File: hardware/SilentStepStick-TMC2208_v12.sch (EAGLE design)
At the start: 26 parts, among them IC1 TMC2208, J1 JUMPER2-0402, J2 JUMPER3-0402-NC, X1 PASSER-04, X2 PASSER-04

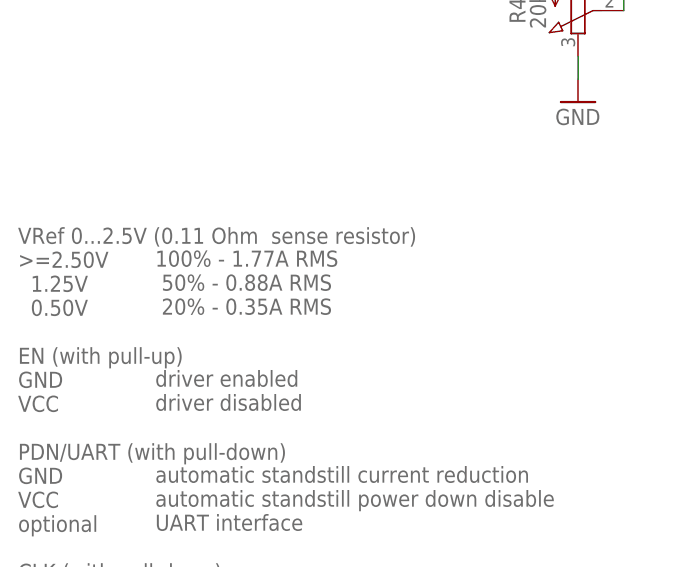
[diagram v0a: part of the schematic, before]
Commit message: corrected Vref and current values
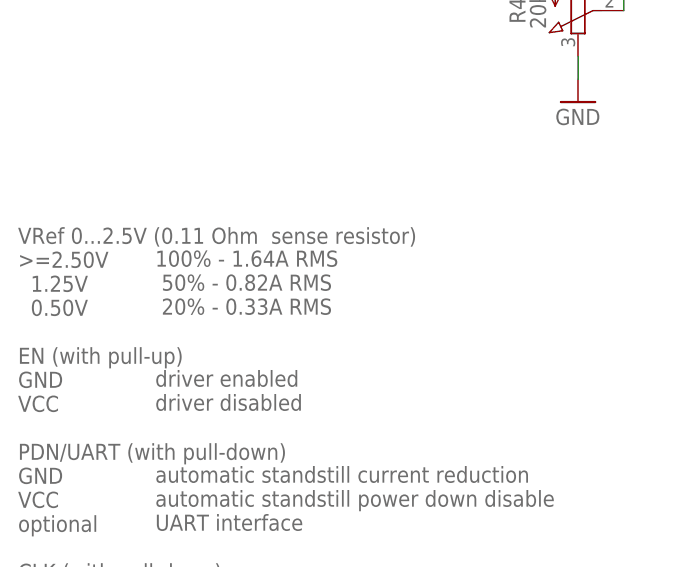
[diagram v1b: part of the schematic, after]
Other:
- note added: "100% - 1.64A RMS 50% - 0.82A RMS 20% - 0.33A RMS driver enabled driver disabled automatic standstill current reduction automatic standstill power down disable UART interface internal clock supply external clock"
- note removed: "100% - 1.77A RMS 50% - 0.88A RMS 20% - 0.35A RMS driver enabled driver disabled automatic standstill current reduction automatic standstill power down disable UART interface internal clock supply external clock"
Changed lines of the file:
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@@
 GND
 optional</text>
-<text x="38.1" y="55.88" size="1.778" layer="95" font="vector" ratio="10" align="top-left">100% - 1.77A RMS
- 50% - 0.88A RMS
- 20% - 0.35A RMS
+<text x="38.1" y="55.88" size="1.778" layer="95" font="vector" ratio="10" align="top-left">100% - 1.64A RMS
+ 50% - 0.82A RMS
+ 20% - 0.33A RMS
 driver enabled
 driver disabled
